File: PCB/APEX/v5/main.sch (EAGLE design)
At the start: 6 parts

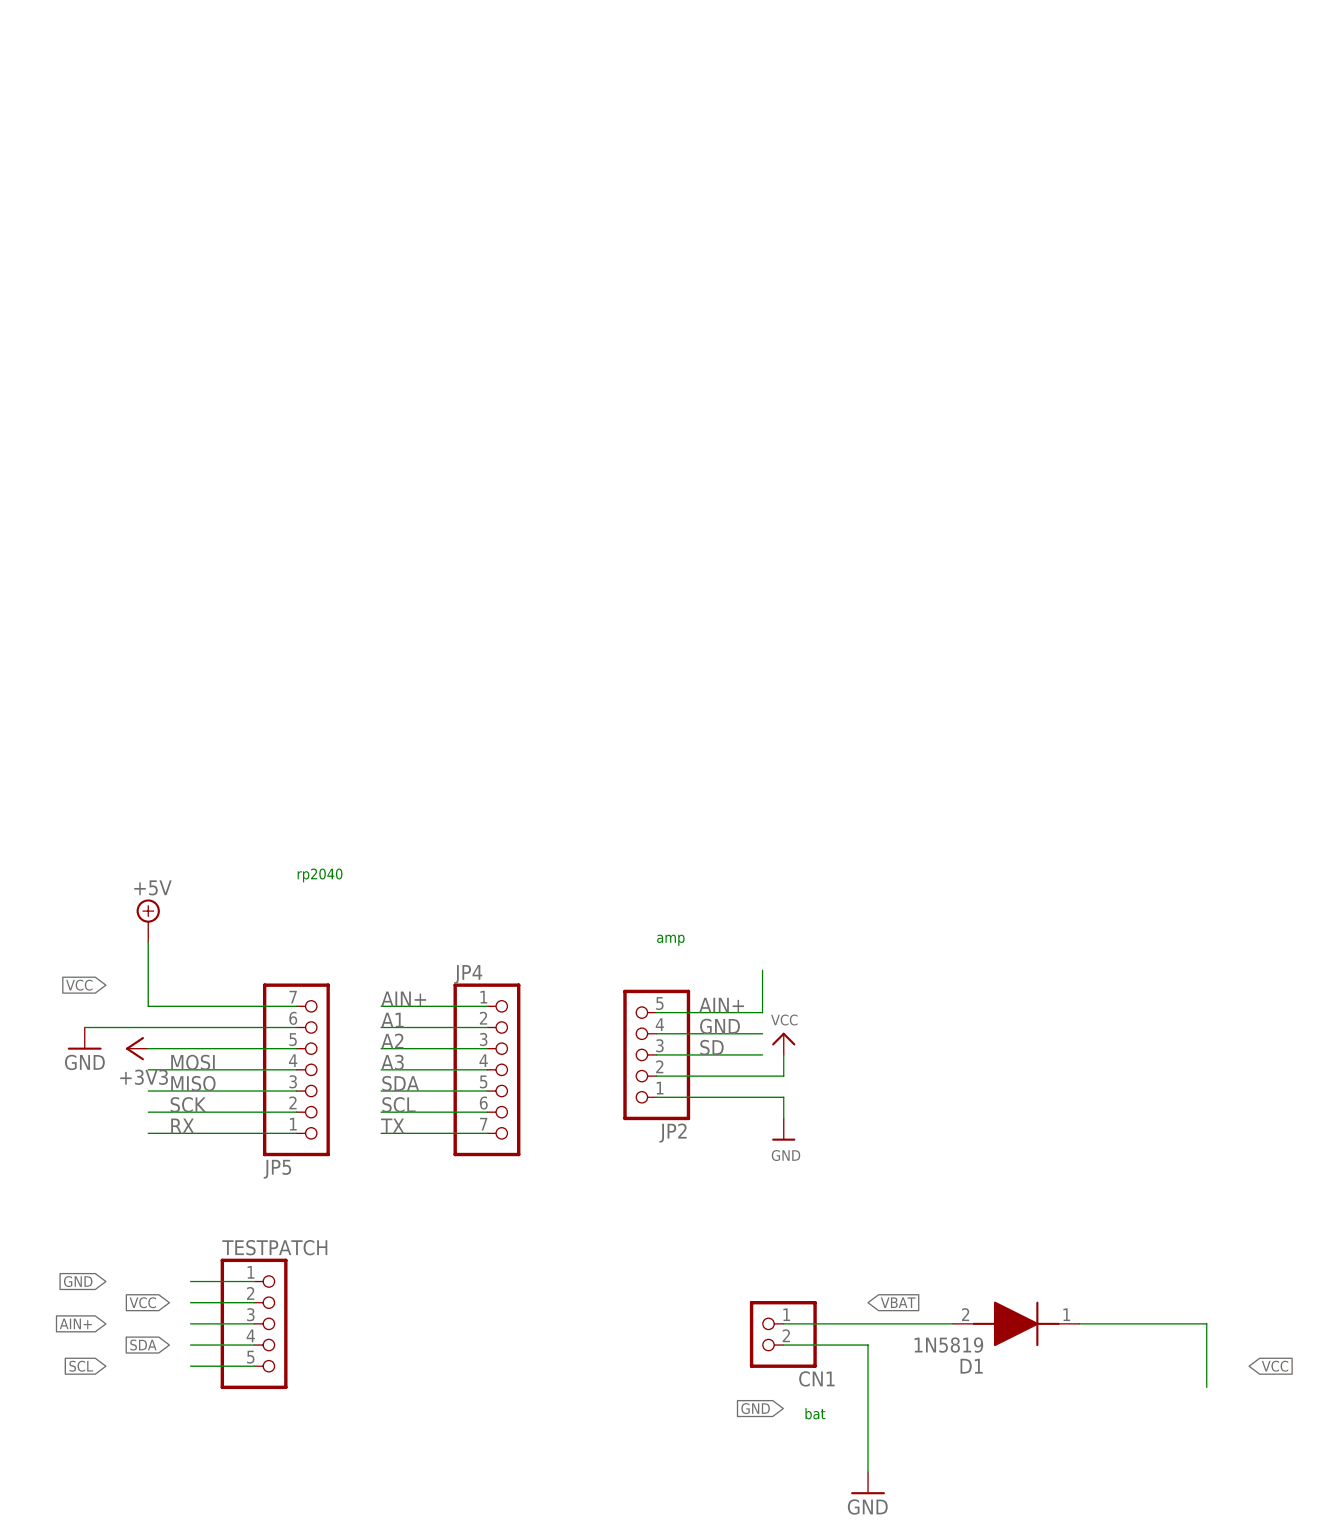
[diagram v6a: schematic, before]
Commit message: remove adafruit frame
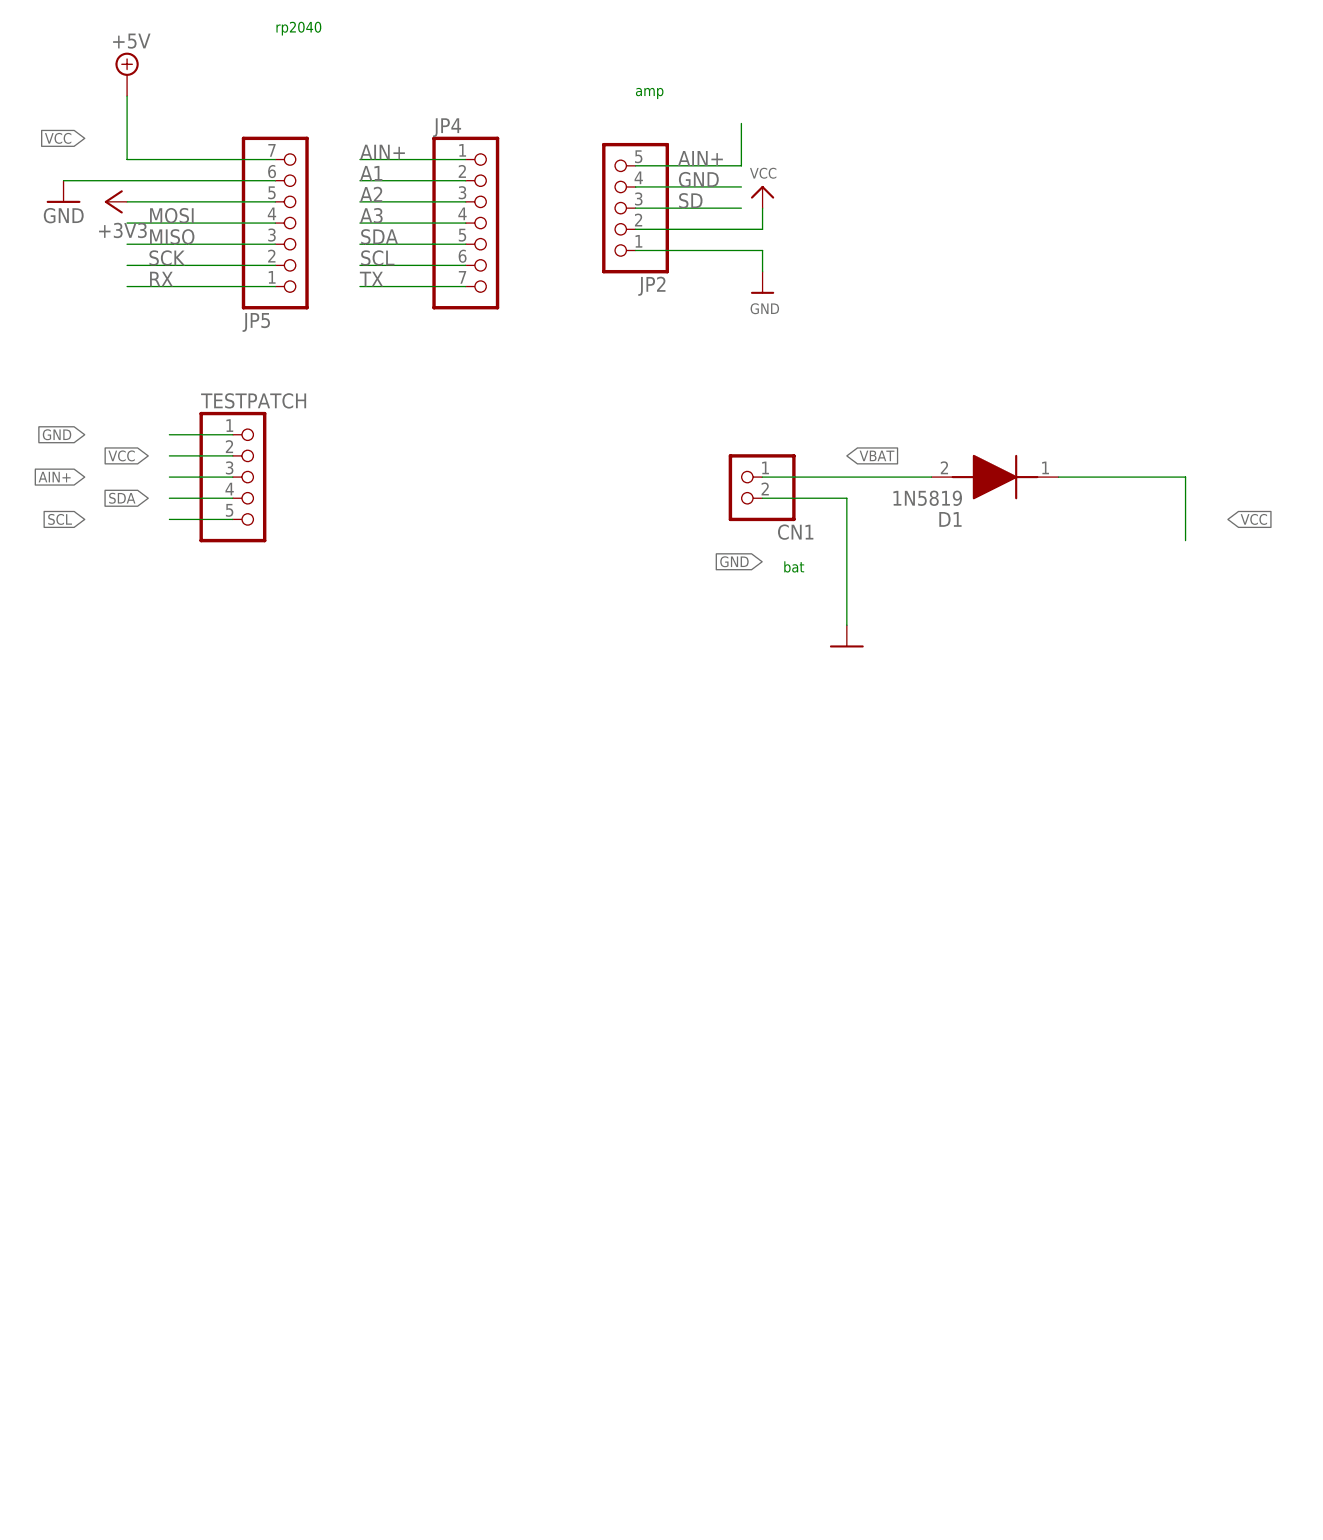
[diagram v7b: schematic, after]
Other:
- moved on the sheet: CN1, D1, JP2, JP4, JP5, TESTPATCH
